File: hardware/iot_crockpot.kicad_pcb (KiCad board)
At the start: 2 copper layers, 10 parts, among them K1 G5LE-1, K2 G5LE-1, Q1 2N7002, Q2 2N7002, U1 AMS1117-3.3, U2 MOUDLE-SEEEDUINO-XIAO-ESP32C3, U3 MAX31855KASA

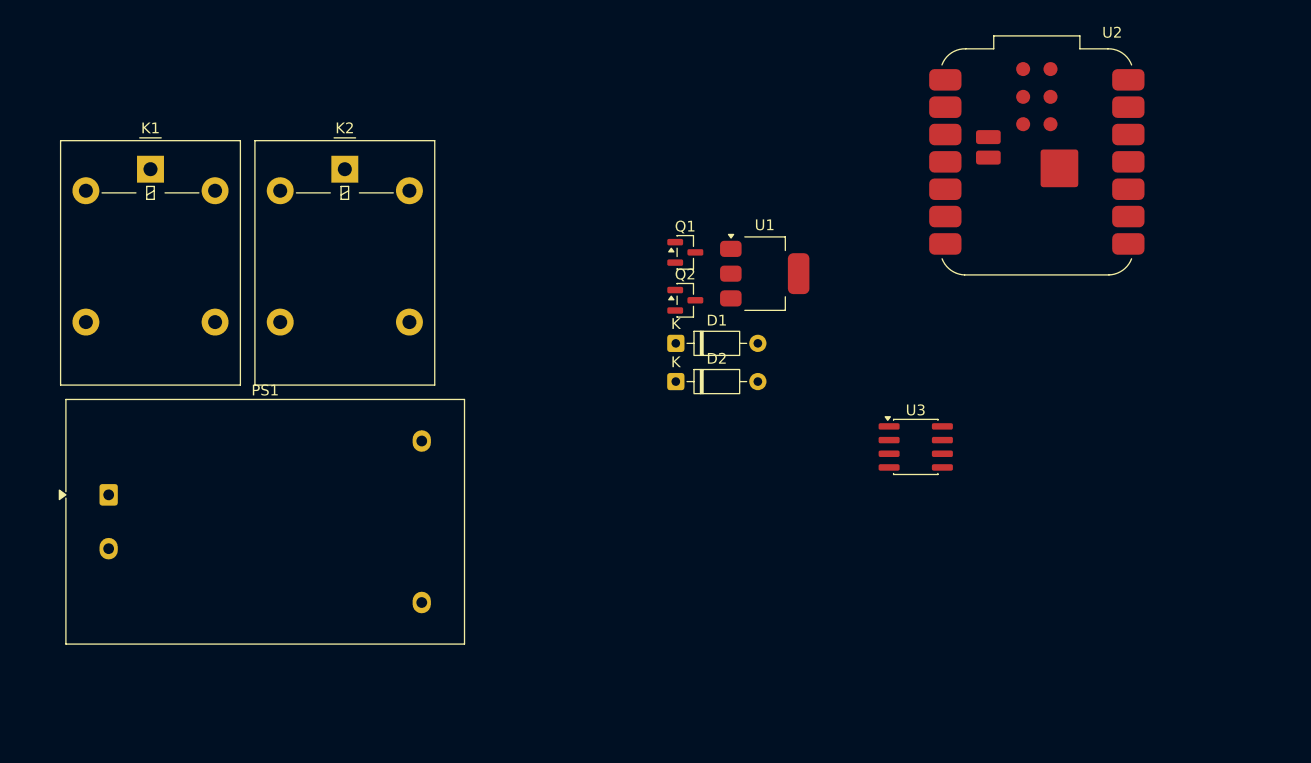
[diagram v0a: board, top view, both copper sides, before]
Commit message: Schematic Updates - Power Supply
Added architecture for power supply to schematic.
Need to rethink control architecture. There is only two I/O exposed on
CYD. May use second MCU on control board flashed and controlled over
I2C by CYD.
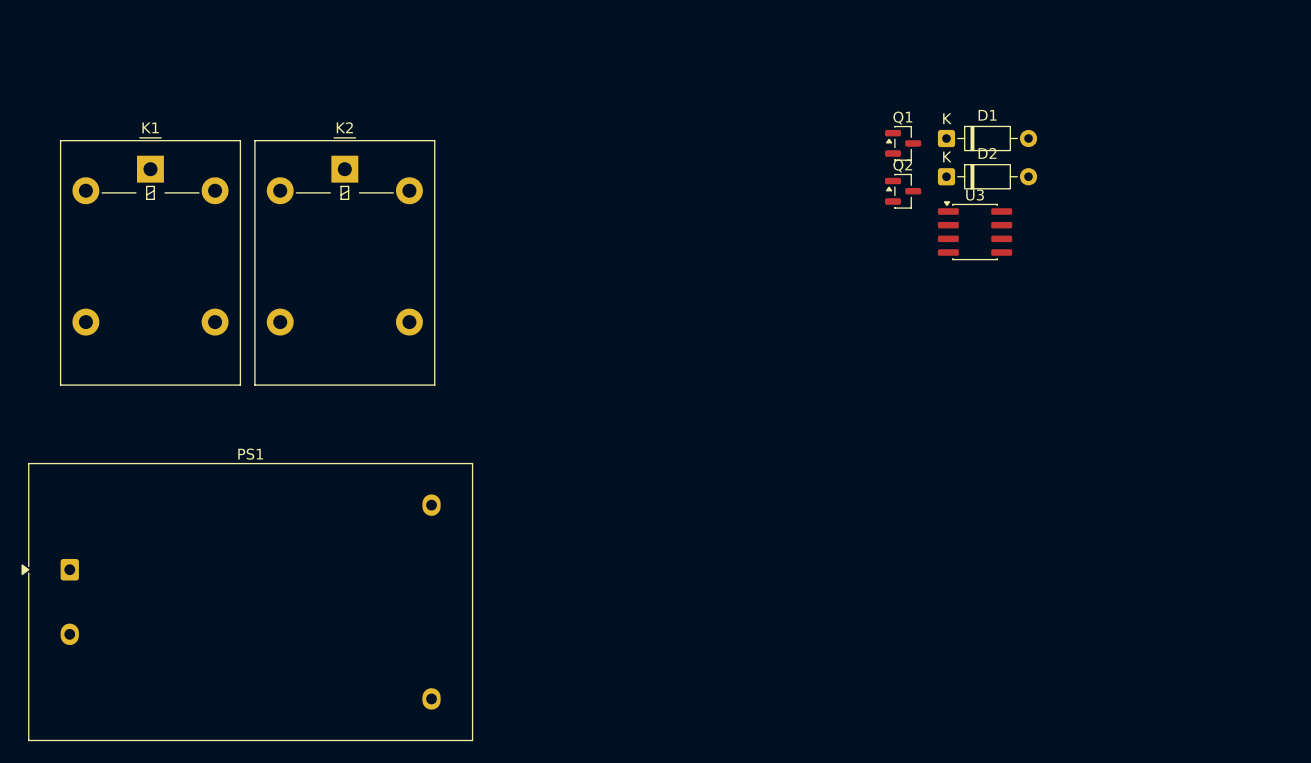
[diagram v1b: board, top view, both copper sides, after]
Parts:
- removed U1: AMS1117-3.3, Package_TO_SOT_SMD:SOT-223-3_TabPin2
- removed U2: MOUDLE-SEEEDUINO-XIAO-ESP32C3, XIAO-ESP32-C3:MCU_Seeed_ESP32C3_w_3D_model
- PS1: value HLK-PM01 -> HLK-5M05; footprint Converter_ACDC:Converter_ACDC_Hi-Link_HLK-PMxx -> Converter_ACDC:Converter_ACDC_Hi-Link_HLK-5Mxx
- moved D2 31.5 mm to (167.9, 85.5)
- moved D1 31.5 mm to (167.9, 82.0)
- moved Q1 22.6 mm to (163.8, 82.4)
- moved Q2 22.6 mm to (163.8, 86.8)
- moved U3 20.7 mm to (170.5, 90.6)
- moved PS1 7.84 mm to (86.5, 122.0)
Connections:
- D1 pad 1: unconnected-(D1-K-Pad1) -> +5V
- D1 pad 2: unconnected-(D1-A-Pad2) -> Net-(D1-A)
- D2 pad 1: unconnected-(D2-K-Pad1) -> +5V
- D2 pad 2: unconnected-(D2-A-Pad2) -> Net-(D2-A)
- K1 pad 2: unconnected-(K1-Pad2) -> Net-(D1-A)
- K1 pad 5: unconnected-(K1-Pad5) -> +5V
- K2 pad 2: unconnected-(K2-Pad2) -> Net-(D2-A)
- K2 pad 5: unconnected-(K2-Pad5) -> +5V
- Q1 pad 3: unconnected-(Q1-D-Pad3) -> Net-(D2-A)
- Q2 pad 3: unconnected-(Q2-D-Pad3) -> Net-(D1-A)
- U3 pad 6: unconnected-(U3-~{CS}-Pad6) -> Net-(U3-~{CS})

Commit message: More Passive Part Selection
Added passive parts/numbers and models to schematic.
Started rough outline of PCB. Considerations will need to be done for
angle of display in relation to height of components.
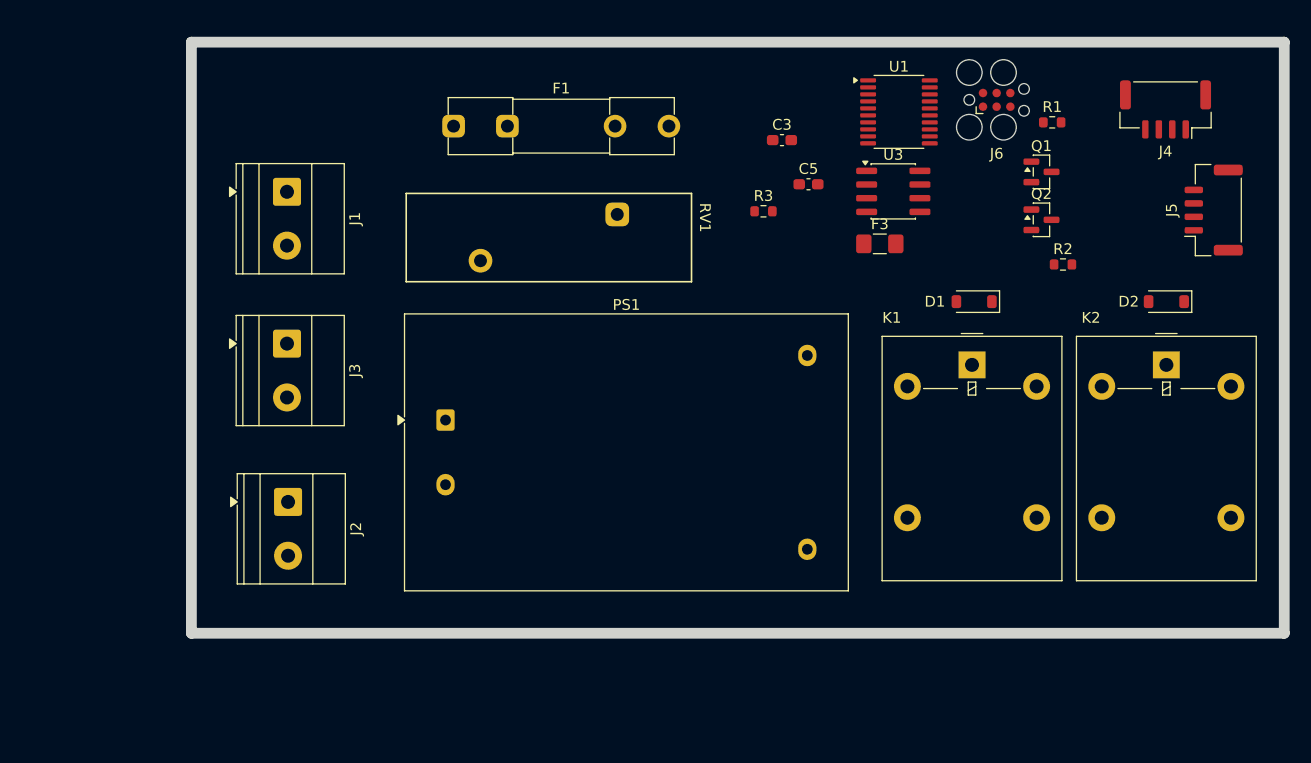
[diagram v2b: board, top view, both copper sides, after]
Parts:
- added C3: 0.1uF, Capacitor_SMD:C_0603_1608Metric_Pad1.08x0.95mm_HandSolder, F.Cu at (152.6, 82.1)
- added C5: 0.1uF, Capacitor_SMD:C_0603_1608Metric_Pad1.08x0.95mm_HandSolder, F.Cu at (155.1, 86.2)
- added F1: Fuse, Fuses:Fuseholder_Clip-5x20mm_Littelfuse_111_Inline_P20.00x5.00mm_D1.05mm_Horizontal_with_3D_body, F.Cu at (122.1, 80.8)
- added F3: 1.5A, Fuse:Fuse_1206_3216Metric_Pad1.42x1.75mm_HandSolder, F.Cu at (161.7, 91.7)
- added J1: Screw_Terminal_01x02, TerminalBlock_Phoenix:TerminalBlock_Phoenix_MKDS-1,5-2_1x02_P5.00mm_Horizontal, F.Cu at (106.6, 86.9)
- added J2: Screw_Terminal_01x02, TerminalBlock_Phoenix:TerminalBlock_Phoenix_MKDS-1,5-2_1x02_P5.00mm_Horizontal, F.Cu at (106.7, 115.7)
- added J3: Screw_Terminal_01x02, TerminalBlock_Phoenix:TerminalBlock_Phoenix_MKDS-1,5-2_1x02_P5.00mm_Horizontal, F.Cu at (106.6, 101.0)
- added J4: Conn_01x04_Pin, Connector_JST:JST_GH_SM04B-GHS-TB_1x04-1MP_P1.25mm_Horizontal, F.Cu at (188.2, 79.2)
- added J5: Conn_01x04_Pin, Connector_JST:JST_GH_SM04B-GHS-TB_1x04-1MP_P1.25mm_Horizontal, F.Cu at (192.7, 88.6)
- added J6: Conn_ARM_SWD_TagConnect_TC2030, Connector:Tag-Connect_TC2030-IDC-FP_2x03_P1.27mm_Vertical, F.Cu at (172.5, 78.4)
- added R1: 10k, Resistor_SMD:R_0603_1608Metric, F.Cu at (177.7, 80.5)
- added R2: 10k, Resistor_SMD:R_0603_1608Metric, F.Cu at (178.7, 93.7)
- added R3: 10k, Resistor_SMD:R_0603_1608Metric, F.Cu at (150.9, 88.7)
- added RV1: Varistor, Varistor:RV_Rect_V25S440P_L26.5mm_W8.2mm_P12.7mm, F.Cu at (137.3, 89.0)
- added U1: STM32G031F6Px, Package_SO:TSSOP-20_4.4x6.5mm_P0.65mm, F.Cu at (163.5, 79.5)
- D1, D2: value 1N4148 -> 1N4148W; footprint Diode_THT:D_DO-35_SOD27_P7.62mm_Horizontal -> Diode_SMD:D_SOD-123
- K1, K2: value G5LE-1 -> G5LE-14 5VDC
- moved K2 78.4 mm to (188.3, 103.0)
- moved K1 78.4 mm to (170.2, 103.0)
- moved PS1 37.6 mm to (121.4, 108.1)
- moved D2 23.5 mm to (188.3, 97.1), turned to 180 degrees
- moved D1 15.4 mm to (170.4, 97.1), turned to 180 degrees
- moved Q2 13.1 mm to (176.7, 89.5)
- moved Q1 13.1 mm to (176.7, 85.0)
- moved U3 8.48 mm to (162.9, 86.9)
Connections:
- K1 pad 1: unconnected-(K1-Pad1) -> /RELAY_HOT
- K1 pad 4: unconnected-(K1-Pad4) -> Net-(J2-Pin_1)
- K2 pad 1: unconnected-(K2-Pad1) -> /RELAY_HOT
- K2 pad 4: unconnected-(K2-Pad4) -> Net-(J2-Pin_2)
- PS1 pad 1: unconnected-(PS1-AC/L-Pad1) -> Net-(PS1-AC/L)
- PS1 pad 2: unconnected-(PS1-AC/N-Pad2) -> Net-(PS1-AC/N)
- PS1 pad 3: unconnected-(PS1--Vout-Pad3) -> GND
- PS1 pad 4: unconnected-(PS1-+Vout-Pad4) -> Net-(PS1-+Vout)
- Q1 pad 1: Net-(Q1-G) -> /RELAY_2
- Q2 pad 1: Net-(Q2-G) -> /RELAY_1
- U3 pad 2: unconnected-(U3-T--Pad2) -> Net-(J3-Pin_1)
- U3 pad 3: unconnected-(U3-T+-Pad3) -> Net-(J3-Pin_2)
- U3 pad 5: unconnected-(U3-SCK-Pad5) -> /SPI1_SCK
- U3 pad 6: Net-(U3-~{CS}) -> /MAX31855_CS_N
- U3 pad 7: unconnected-(U3-SO-Pad7) -> /SPI1_MISO
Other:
- board outline added: 101.5 x 54.9 mm

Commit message: Edited JST Connectors and created 3D model
Edited JST Connectors and created 3D model for use in
Fusion 360. This will drive where tall components will be placed on
PCB.
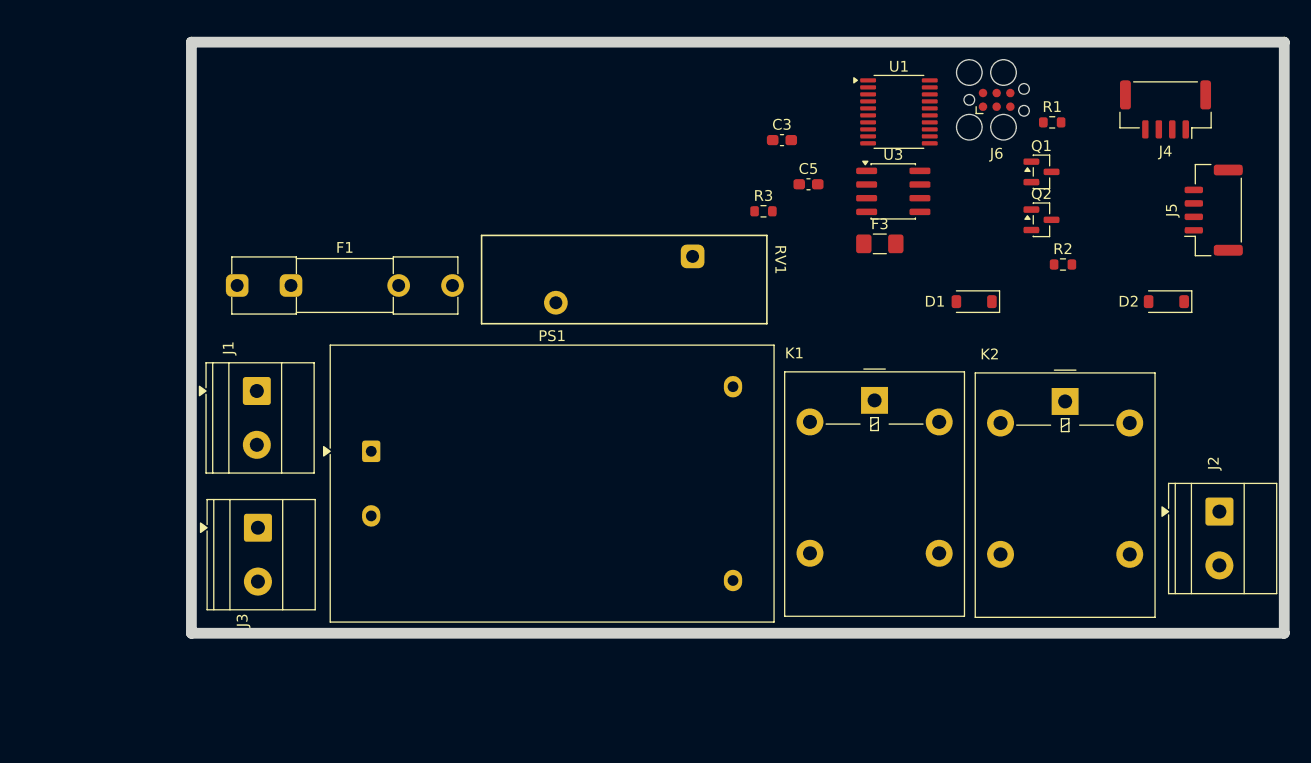
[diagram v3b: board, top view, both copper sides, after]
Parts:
- moved J2 86.5 mm to (193.2, 116.6)
- moved F1 25.0 mm to (102.0, 95.6)
- moved J1 18.7 mm to (103.8, 105.4)
- moved J3 17.3 mm to (103.9, 118.1)
- moved K2 10.00 mm to (178.9, 106.4)
- moved K1 9.63 mm to (161.2, 106.3)
- moved RV1 8.01 mm to (144.3, 92.9)
- moved PS1 7.48 mm to (114.5, 111.0)
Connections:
- J6 pad 1: unconnected-(J6-VCC-Pad1) -> +3V3
- J6 pad 5: unconnected-(J6-GND-Pad5) -> GND
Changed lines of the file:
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@@
 	(net 44 "unconnected-(J5-Pin_2-Pad2)")
 	(net 45 "unconnected-(J5-Pin_3-Pad3)")
-	(net 46 "unconnected-(J6-GND-Pad5)")
-	(net 47 "unconnected-(J6-SWO-Pad6)")
-	(net 48 "unconnected-(J6-SWDIO-Pad2)")
-	(net 49 "unconnected-(J6-SWCLK-Pad4)")
-	(net 50 "unconnected-(J6-~{RESET}-Pad3)")
-	(net 51 "unconnected-(J6-VCC-Pad1)")
+	(net 46 "unconnected-(J6-SWO-Pad6)")
+	(net 47 "unconnected-(J6-SWDIO-Pad2)")
+	(net 48 "unconnected-(J6-SWCLK-Pad4)")
+	(net 49 "unconnected-(J6-~{RESET}-Pad3)")
 	(footprint "Package_SO:TSSOP-20_4.4x6.5mm_P0.65mm"
 		(layer "F.Cu")
@@
 			(size 0.7874 0.7874)
 			(layers "F.Cu" "F.Mask")
-			(net 51 "unconnected-(J6-VCC-Pad1)")
+			(net 18 "+3V3")
 			(pinfunction "VCC")
 			(pintype "power_in")
@@
 			(size 0.7874 0.7874)
 			(layers "F.Cu" "F.Mask")
-			(net 48 "unconnected-(J6-SWDIO-Pad2)")
+			(net 47 "unconnected-(J6-SWDIO-Pad2)")
 			(pinfunction "SWDIO")
 			(pintype "bidirectional")
@@
 			(size 0.7874 0.7874)
 			(layers "F.Cu" "F.Mask")
-			(net 50 "unconnected-(J6-~{RESET}-Pad3)")
+			(net 49 "unconnected-(J6-~{RESET}-Pad3)")
 			(pinfunction "~{RESET}")
 			(pintype "open_collector")
@@
 			(size 0.7874 0.7874)
 			(layers "F.Cu" "F.Mask")
-			(net 49 "unconnected-(J6-SWCLK-Pad4)")
+			(net 48 "unconnected-(J6-SWCLK-Pad4)")
 			(pinfunction "SWCLK")
 			(pintype "output")
@@
 			(size 0.7874 0.7874)
 			(layers "F.Cu" "F.Mask")
-			(net 46 "unconnected-(J6-GND-Pad5)")
+			(net 16 "GND")
 			(pinfunction "GND")
 			(pintype "power_in")
@@
 			(size 0.7874 0.7874)
 			(layers "F.Cu" "F.Mask")
-			(net 47 "unconnected-(J6-SWO-Pad6)")
+			(net 46 "unconnected-(J6-SWO-Pad6)")
 			(pinfunction "SWO")
 			(pintype "input")
@@
 	(footprint "Varistor:RV_Rect_V25S440P_L26.5mm_W8.2mm_P12.7mm"
 		(layer "F.Cu")
-		(at 137.3 89 -90)
+		(at 144.3 92.9 -90)
 		(descr "Varistor, V25S440P, https://www.littelfuse.com/media?resourcetype=datasheets&itemid=b410c42c-51d1-460e-b1d9-d105d93c9679&filename=littelfuse-varistor-ultramov25s-datasheet")
 		(tags "varistor")
@@
 		)
 		(property "Value" "Varistor"
-			(at 1.7 6.5 270)
+			(at 2.15 6.35 270)
 			(unlocked yes)
 			(layer "F.Fab")
@@
 	(footprint "TerminalBlock_Phoenix:TerminalBlock_Phoenix_MKDS-1,5-2_1x02_P5.00mm_Horizontal"
 		(layer "F.Cu")
-		(at 106.6275 101 -90)
+		(at 103.9275 118.1 -90)
 		(descr "Terminal Block Phoenix MKDS-1,5-2, 2 pins, pitch 5mm, size 10x9.8mm, drill diameter 1.3mm, pad diameter 2.6mm, http://www.farnell.com/datasheets/100425.pdf, script-generated using https://gitlab.com/kicad/libraries/kicad-footprint-generator/-/tree/master/scripts/TerminalBlock_Phoenix")
 		(tags "THT Terminal Block Phoenix MKDS-1,5-2 pitch 5mm size 10x9.8mm drill 1.3mm pad 2.6mm")
 		(property "Reference" "J3"
-			(at 2.5 -6.32 90)
+			(at 8.6 1.4275 90)
 			(layer "F.SilkS")
 			(effects
@@
 	(footprint "Converter_ACDC:Converter_ACDC_Hi-Link_HLK-5Mxx"
 		(layer "F.Cu")
-		(at 121.3525 108.1)
+		(at 114.4525 111)
 		(descr "ACDC-Converter, 5W, Hi-Link, HLK-5Mxx, THT, https://h.hlktech.com/download/ACDC%E7%94%B5%E6%BA%90%E6%A8%A1%E5%9D%975W%E7%B3%BB%E5%88%97/1/%E6%B5%B7%E5%87%8C%E7%A7%915W%E7%B3%BB%E5%88%97%E7%94%B5%E6%BA%90%E6%A8%A1%E5%9D%97%E8%A7%84%E6%A0%BC%E4%B9%A6V2.8.pdf, generated with kicad-footprint-generator StandardBox_generator.py")
 		(tags "ACDC-Converter 5W THT Hi-Link board mount module")
@@
 	(footprint "Relay_THT:Relay_SPDT_Omron-G5LE-1"
 		(layer "F.Cu")
-		(at 170.25 102.9725)
+		(at 161.2 106.2725)
 		(descr "Omron Relay SPDT, http://www.omron.com/ecb/products/pdf/en-g5le.pdf")
 		(tags "Omron Relay SPDT")
@@
 	(footprint "TerminalBlock_Phoenix:TerminalBlock_Phoenix_MKDS-1,5-2_1x02_P5.00mm_Horizontal"
 		(layer "F.Cu")
-		(at 106.6275 86.9 -90)
+		(at 103.8275 105.4 -90)
 		(descr "Terminal Block Phoenix MKDS-1,5-2, 2 pins, pitch 5mm, size 10x9.8mm, drill diameter 1.3mm, pad diameter 2.6mm, http://www.farnell.com/datasheets/100425.pdf, script-generated using https://gitlab.com/kicad/libraries/kicad-footprint-generator/-/tree/master/scripts/TerminalBlock_Phoenix")
 		(tags "THT Terminal Block Phoenix MKDS-1,5-2 pitch 5mm size 10x9.8mm drill 1.3mm pad 2.6mm")
 		(property "Reference" "J1"
-			(at 2.5 -6.32 90)
+			(at -4 2.6275 90)
 			(layer "F.SilkS")
 			(effects
@@
 	(footprint "Fuses:Fuseholder_Clip-5x20mm_Littelfuse_111_Inline_P20.00x5.00mm_D1.05mm_Horizontal_with_3D_body"
 		(layer "F.Cu")
-		(at 122.1 80.8)
+		(at 102 95.6)
 		(descr "Fuseholder Clips, 5x20mm Cylinder Fuse, Pins Inline, Horizontal, Littelfuse 111, https://m.littelfuse.com/~/media/electronics/datasheets/fuse_clips/littelfuse_fuse_clip_111_519_datasheet.pdf.pdf")
 		(tags "fuse clip open")
@@
 	(footprint "Relay_THT:Relay_SPDT_Omron-G5LE-1"
 		(layer "F.Cu")
-		(at 188.3 102.9725)
+		(at 178.9 106.3725)
 		(descr "Omron Relay SPDT, http://www.omron.com/ecb/products/pdf/en-g5le.pdf")
 		(tags "Omron Relay SPDT")
@@
 	(footprint "TerminalBlock_Phoenix:TerminalBlock_Phoenix_MKDS-1,5-2_1x02_P5.00mm_Horizontal"
 		(layer "F.Cu")
-		(at 106.7275 115.7 -90)
+		(at 193.2275 116.6 -90)
 		(descr "Terminal Block Phoenix MKDS-1,5-2, 2 pins, pitch 5mm, size 10x9.8mm, drill diameter 1.3mm, pad diameter 2.6mm, http://www.farnell.com/datasheets/100425.pdf, script-generated using https://gitlab.com/kicad/libraries/kicad-footprint-generator/-/tree/master/scripts/TerminalBlock_Phoenix")
 		(tags "THT Terminal Block Phoenix MKDS-1,5-2 pitch 5mm size 10x9.8mm drill 1.3mm pad 2.6mm")
 		(property "Reference" "J2"
-			(at 2.5 -6.32 90)
+			(at -4.5 0.5275 90)
 			(layer "F.SilkS")
 			(effects
